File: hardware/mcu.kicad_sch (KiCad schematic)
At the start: 25 parts, among them U6 T113-S3

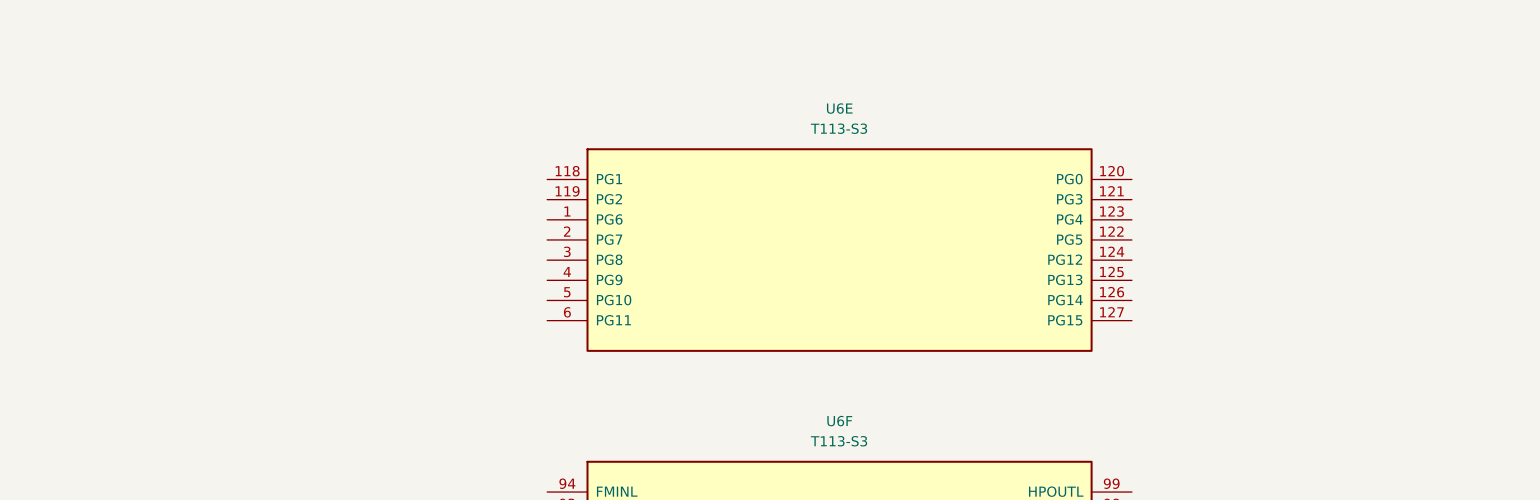
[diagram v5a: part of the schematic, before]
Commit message: ★ unit 5 完成(16/16):PG 排針,每支串限流電阻
PG0~PG15 全部拉到排針,照 007 §4 規則②:
  I2C ×2 (PG7/PG8 TWI2、PG9/PG10 TWI1)   100R
  其餘 12 支                              330R
標籤用 HDR_ 前綴 —— layout 階段能一眼認出哪些 net 是對外的
(要串電阻、要在 PG bank、要遠離高速差分)。

★ 踩到第六次命名坑,形狀跟前五次相反:
  前五次  名字寫錯 → 該連的沒連 → 留下孤立 net,檢查得到
  這次    PG0 與 PG1 都標成 HDR_GPIO2 → 不該連的連在一起
          兩支 GPIO 經各自的 330R 併在一起,軟體一高一低就有 5mA 穿流,
          而且少一個對外接點、GPIO4 憑空消失
  後者更危險:netlist 完全合法、看起來一切正常,只有逐一比對才抓得到。

check_power_rails.py 兩項擴充:
  ① 新增「同一條訊號 net 掛多顆電阻」檢查(HDR_/LCD0_/DSI_/SDC0_/SPI0_/RMII_),
     已用假 netlist 驗證會抓到
  ② 跨頁白名單補 RMII_* 10 條、PHY_RESET_N、HDR_* 16 條

另:這次把「KiCad 開著就中止」寫成硬性 exit,不再只印警告 ——
上一輪自己違反了剛寫的 012 §6.2,教訓是警告訊息不是防護措施。

U6 進度:98 / 129 腳。

Co-Authored-By: Claude Opus 5 <noreply@anthropic.com>
Claude-Session: https://claude.ai/code/session_01HtGUWSQFey6W2g2grqgTMR
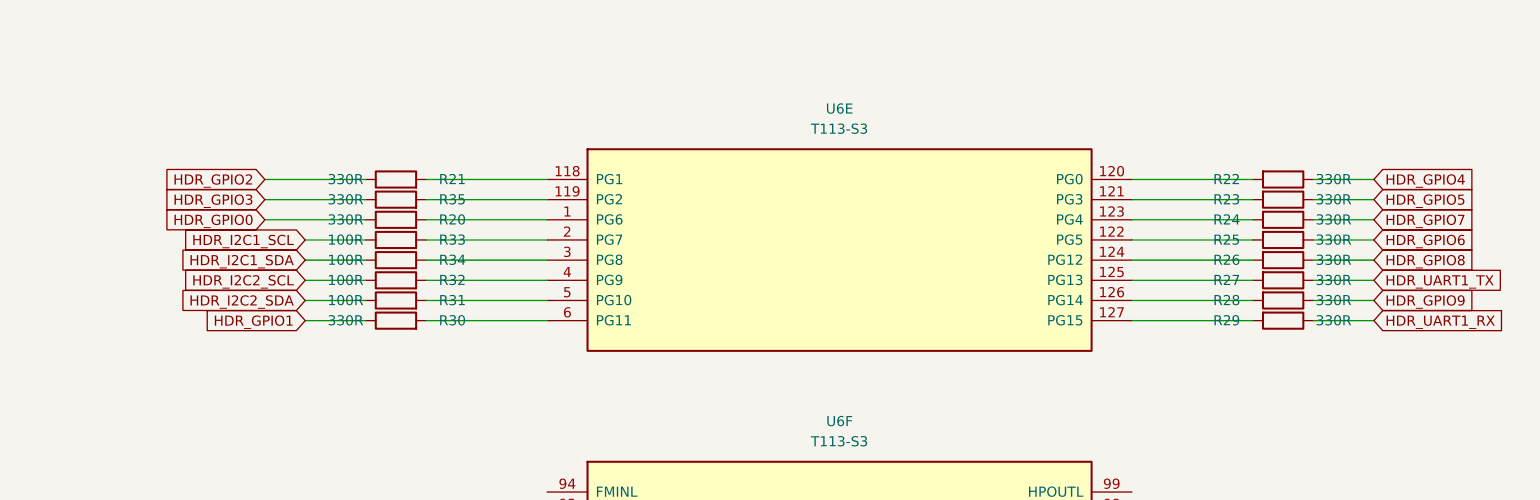
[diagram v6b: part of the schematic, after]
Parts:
- added R20, R21, R22, R23, R24, R25, R26, R27, R28, R29, R30, R35: 330R, symbol Device:R
- added R31, R32, R33, R34: 100R, symbol Device:R
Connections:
- net at U6.1 (PG6): now also R20.2
- net at U6.118 (PG1): now also R21.2
- net at U6.119 (PG2): now also R35.2
- net at U6.120 (PG0): now also R22.2
- net at U6.121 (PG3): now also R23.2
- net at U6.122 (PG5): now also R25.2
- net at U6.123 (PG4): now also R24.2
- net at U6.124 (PG12): now also R26.2
- net at U6.125 (PG13): now also R27.2
- net at U6.126 (PG14): now also R28.2
- net at U6.127 (PG15): now also R29.2
- net at U6.2 (PG7): now also R33.2
- net at U6.3 (PG8): now also R34.2
- net at U6.4 (PG9): now also R32.2
- net at U6.5 (PG10): now also R31.2
- net at U6.6 (PG11): now also R30.2
- new net HDR_GPIO0: R20.1
- new net HDR_GPIO1: R30.1
- new net HDR_GPIO2: R21.1
- new net HDR_GPIO3: R35.1
- new net HDR_GPIO4: R22.1
- new net HDR_GPIO5: R23.1
- new net HDR_GPIO6: R25.1
- new net HDR_GPIO7: R24.1
- new net HDR_GPIO8: R26.1
- new net HDR_GPIO9: R28.1
- new net HDR_I2C1_SCL: R33.1
- new net HDR_I2C1_SDA: R34.1
- new net HDR_I2C2_SCL: R32.1
- new net HDR_I2C2_SDA: R31.1
- new net HDR_UART1_RX: R29.1
- new net HDR_UART1_TX: R27.1

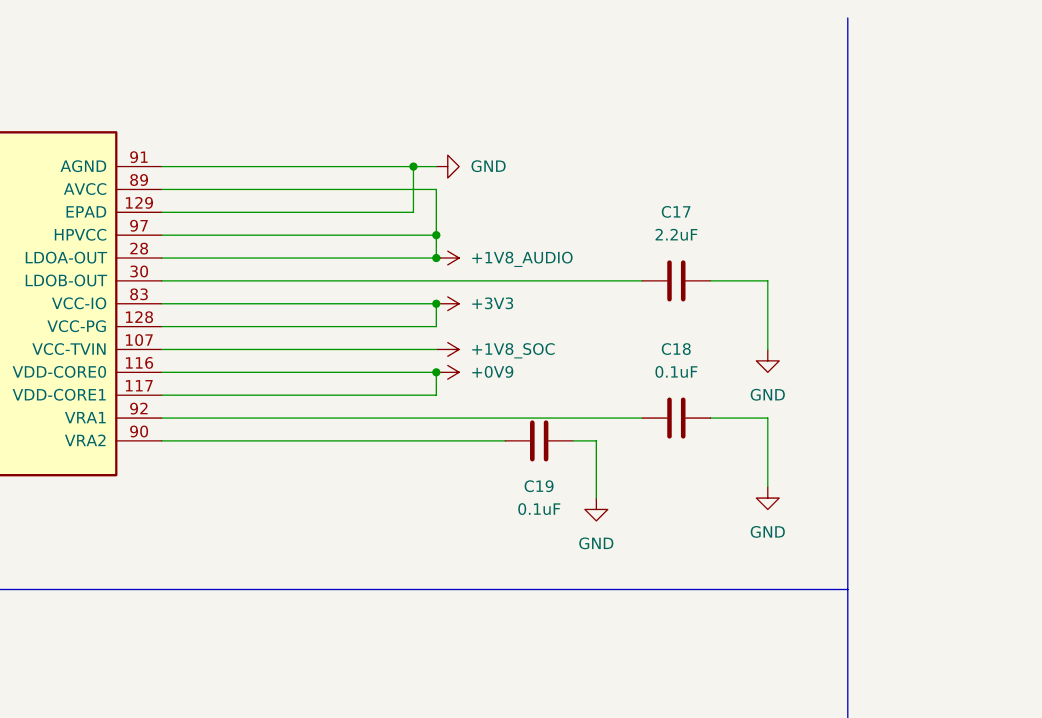
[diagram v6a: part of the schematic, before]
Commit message: 類比地單點接地;VRA 去耦改 0.47uF(對 MangoPi 確認)
查 MangoPi MQ-R v1.6 原理圖 p.3,解開三個 datasheet 沒寫的問題:

  VRA1/VRA2   各 0.47uF 到 AGND(C40/C78)—— 原暫用 0.1uF 是無依據的猜測
  類比地       AGND 經 0R(R15)單點接 GND,不是直接合併
  未用類比腳   FMINL/FMINR 直接打 ✗(No Connect)—— 證明類比輸入可懸空

本板對應的改動:
  C18/C19  0.1uF → 0.47uF,且下端從 GND 移到 AGND
  R36 0R   新增,AGND ←→ GND 單點連接
  EPAD     從 AGND 移出,直接接 GND

★ EPAD 那項是關鍵:它是全晶片唯一的數位地(21 支電源的回流都走它)。
  留在 AGND 上的話,所有數位電流都要擠過 R36 ——
  那顆 0R 的本意只是給類比區一個單點參考,不是當主地線。

★ C18/C19 的下端必須在 AGND 側:
  R36 擋得住數位電流進類比區,但擋不住類比電流跑出去。
  去耦電容的回流點若在數位 GND,0R 就形同虛設(概念 ⑧:回流路徑與供電路徑同等重要)。

另記 MangoPi 原理圖的讀法(整頁 render 看不清,要用文字定位 + 高 dpi 分區裁切),
寫進 docs/reference/README.md。

Co-Authored-By: Claude Opus 5 <noreply@anthropic.com>
Claude-Session: https://claude.ai/code/session_01HtGUWSQFey6W2g2grqgTMR
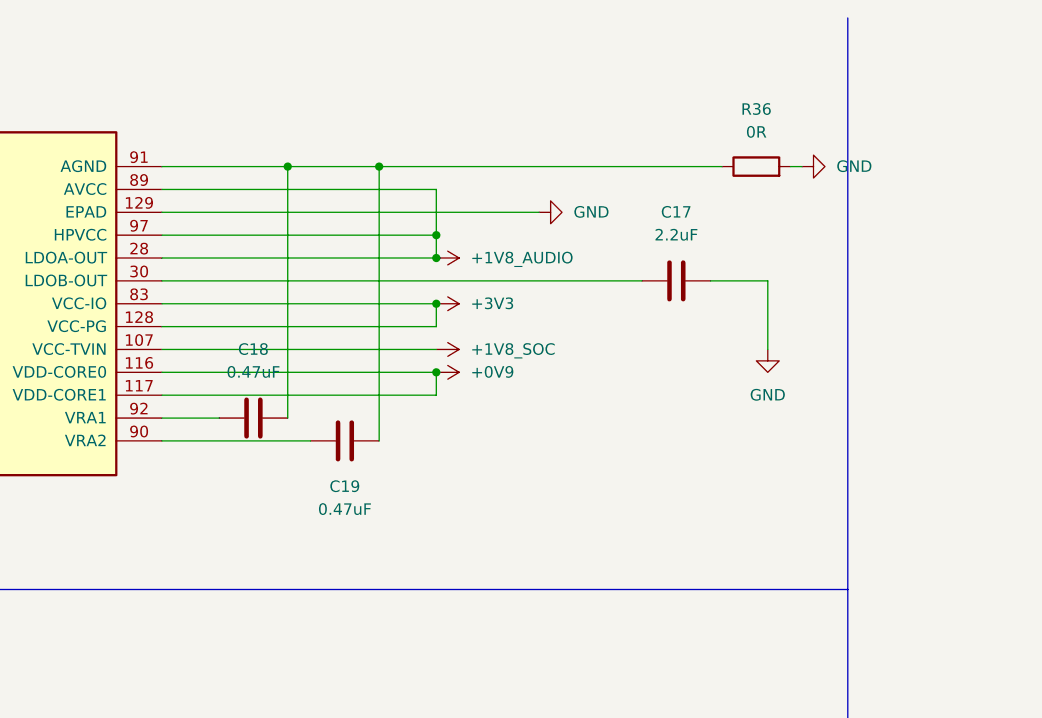
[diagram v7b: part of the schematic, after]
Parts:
- added R36: 0R, symbol Device:R
- C18, C19: value 0.1uF -> 0.47uF
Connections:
- net GND: now also R36.2; no longer C18.1, C19.1, U6.91 (AGND)
- new net: C18.1, C19.1, R36.1, U6.91 (AGND)
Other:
- moved on the sheet: C18, C19
